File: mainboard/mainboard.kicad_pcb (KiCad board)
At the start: 2 copper layers, 116.8 x 73.7 mm, 26 parts, among them J1 Port ESC Connector, J2 Stbd ESC Connector, J3 Battery Connector, J4 RPLIDAR Power Harness, J5 Raspberry_Pi_4

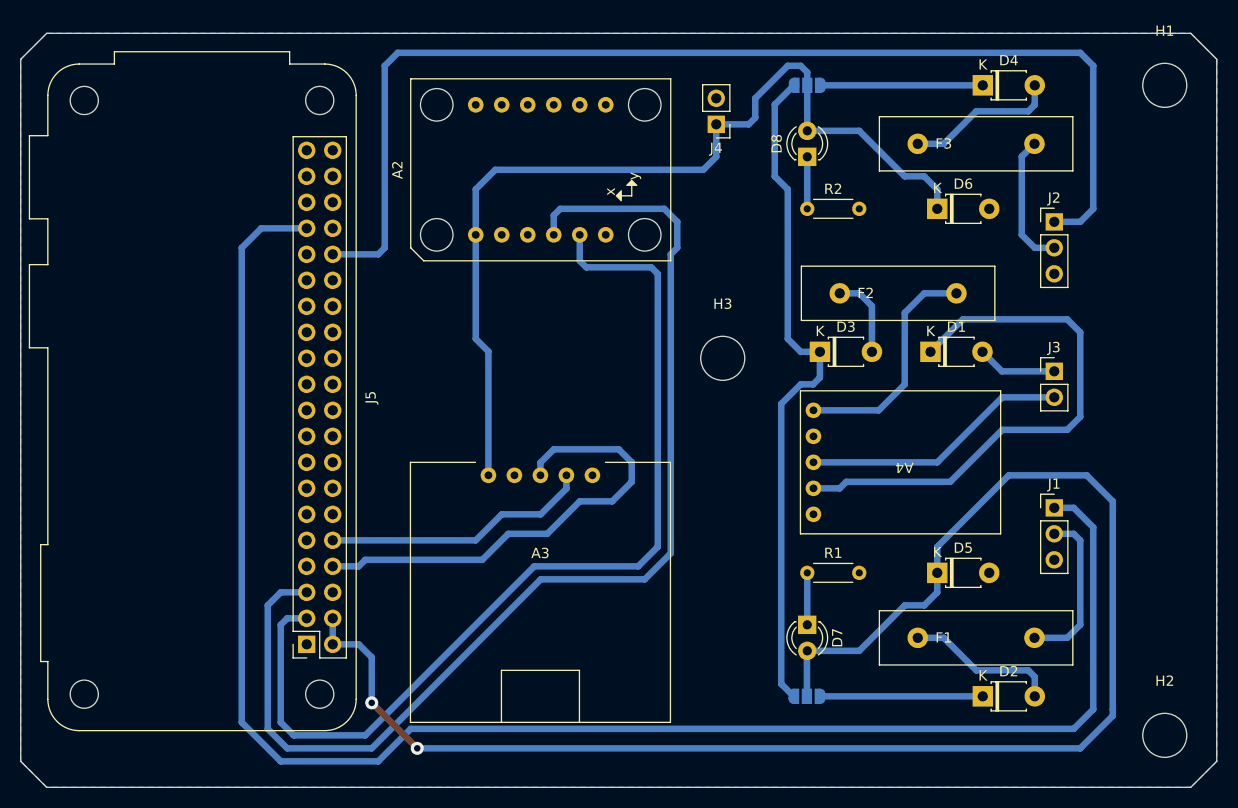
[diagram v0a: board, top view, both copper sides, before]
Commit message: Updated pcb to in spec
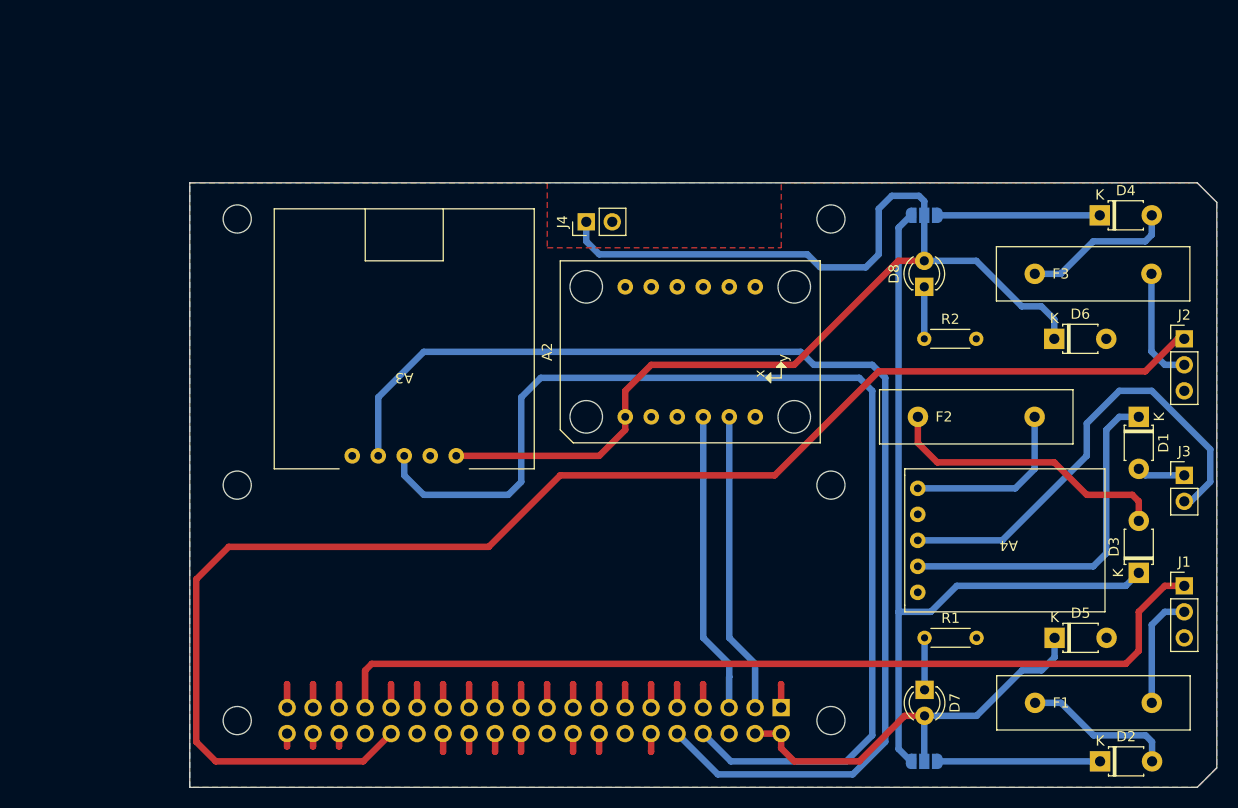
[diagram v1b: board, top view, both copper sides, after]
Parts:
- removed H1, H2, H3: MountingHole, MountingHole:MountingHole_4.3mm_M4
- J5: footprint Module:Raspberry_Pi_Zero_Socketed_THT_FaceDown_MountingHoles -> GTMRG_footprints:RaspberryPi_Multi; moved to B.Cu
- moved D3 37.9 mm to (203.8, 108.6), turned to 90 degrees
- moved A3 28.1 mm to (132.1, 85.7), turned to 180 degrees
- moved A2 23.0 mm to (160.0, 87.0)
- moved J5 22.9 mm to (144.8, 109.9), turned to 90 degrees
- moved D1 21.3 mm to (203.8, 93.3), turned to -90 degrees
- moved D8 17.1 mm to (182.9, 80.6)
- moved D4 17.1 mm to (200.0, 73.7)
- moved JP2 17.1 mm to (182.9, 73.7)
- moved D6 17.1 mm to (195.6, 85.7)
- moved R2 17.1 mm to (182.9, 85.7)
- moved F3 17.1 mm to (205.1, 79.4)
- moved J2 17.1 mm to (208.3, 85.7)
- moved J3 16.3 mm to (208.3, 99.1)
- moved J4 15.9 mm to (149.9, 74.3), turned to 90 degrees
- moved J1 14.8 mm to (208.3, 109.9)
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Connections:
- J5 pad 1: Net-(J5-3V3-Pad1) -> unconnected-(J5-3V3-Pad1)_1
- J5 pad 17: Net-(J5-3V3-Pad1) -> unconnected-(J5-3V3-Pad1)
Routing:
- net +5V_P: track 152.9 -> 41.8 mm, vias 2 -> 0
- net /GPS_TX: track 26.2 -> 117.0 mm
- net /SCL: track 111.9 -> 29.5 mm
- net /PEsc_Sig: track 162.7 -> 89.3 mm
- net /SDA: track 94.7 -> 29.5 mm
- net /GPS_RX: track 45.8 -> 110.9 mm
- net /SEsc_Sig: track 111.7 -> 143.1 mm
- net +5V_S: track 91.8 -> 120.3 mm
- net Net-(D3-A): track 8.13 -> 28.4 mm
- net Net-(A4-IN-): track 26.2 -> 45.4 mm
- net Net-(A4-IN+): track 53.7 -> 34.7 mm
- net Net-(D3-K): track 66.2 -> 79.4 mm
- net GND: track 0.00 -> 6.88 mm
- net +5V_Reg: track 22.8 -> 17.3 mm
- net +5V_PEsc: track 16.1 -> 11.3 mm
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- added copper zone on F.Cu, net GND
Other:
- board size 116.8 x 73.7 mm -> 100.3 x 59.1 mm
- board text removed: "Full Raspberry Pi Approximate Dimensions"

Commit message: Updated to a fabbed PCB
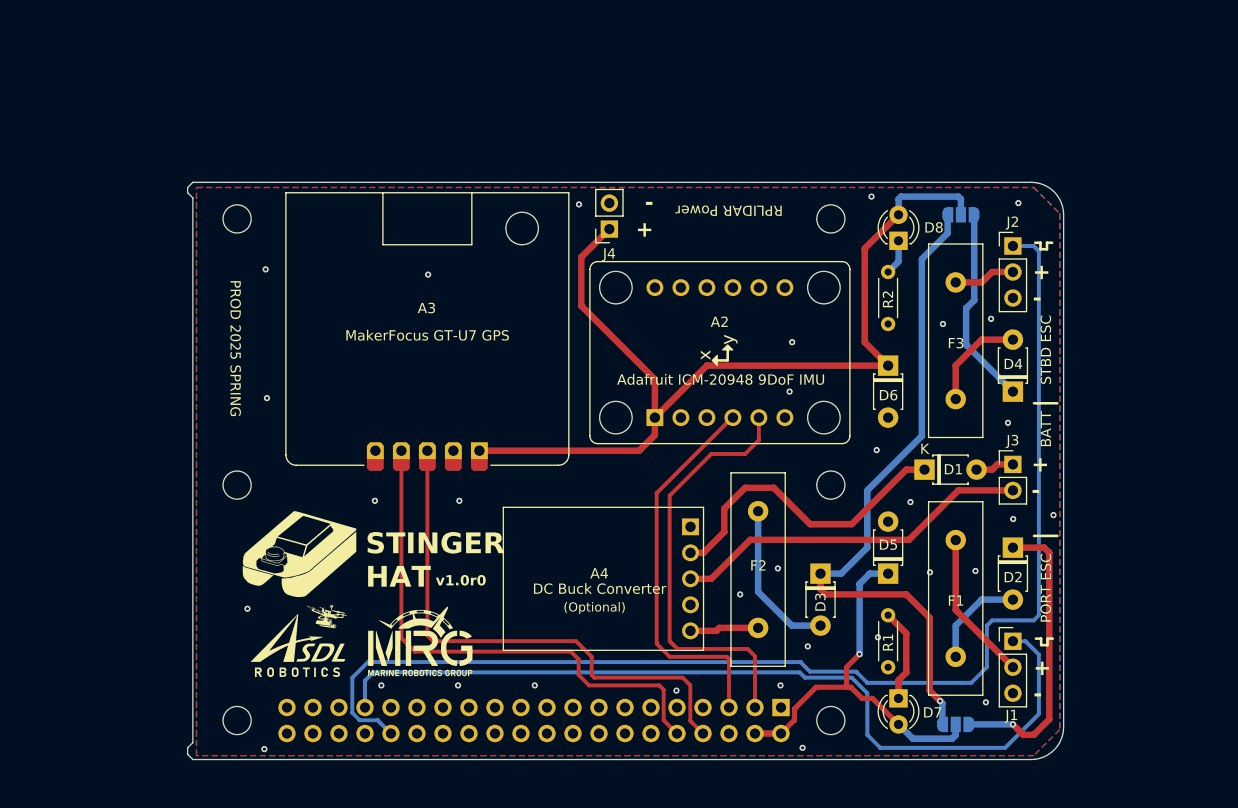
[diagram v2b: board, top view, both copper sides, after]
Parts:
- A4: value DROK DC Buck Converter -> DC Buck Converter
- J4: footprint Connector_PinHeader_2.54mm:PinHeader_1x02_P2.54mm_Vertical -> Connector_PinSocket_2.54mm:PinSocket_1x02_P2.54mm_Vertical
- moved A4 40.2 mm to (151.2, 109.2), turned to 0 degrees
- moved F2 34.0 mm to (166.6, 114.0), turned to 90 degrees
- moved D3 31.1 mm to (172.7, 108.7), turned to -90 degrees
- moved F1 24.9 mm to (186.0, 105.4), turned to -90 degrees
- moved D2 22.5 mm to (191.5, 106.1), turned to -90 degrees
- moved D1 21.6 mm to (182.9, 98.5), turned to 0 degrees
- moved D4 19.2 mm to (191.5, 90.9), turned to 90 degrees
- moved F3 19.1 mm to (186.0, 80.2), turned to -90 degrees
- moved J2 19.0 mm to (191.5, 76.7)
- moved J1 17.6 mm to (191.5, 115.3)
- moved D5 17.4 mm to (179.3, 108.7), turned to 90 degrees
- moved J3 16.8 mm to (191.5, 98.0)
- moved D6 16.4 mm to (179.3, 88.3), turned to -90 degrees
- moved R2 7.42 mm to (179.3, 79.2), turned to -90 degrees
- moved D8 5.15 mm to (180.4, 76.1)
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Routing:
- net /GPS_TX: track 117.0 -> 50.4 mm
- net /GPS_RX: track 110.9 -> 50.7 mm
- net +5V_S: track 120.3 -> 93.3 mm
- net /SEsc_Sig: track 143.1 -> 120.0 mm
- net Net-(D3-K): track 79.4 -> 65.7 mm, vias 0 -> 1
- net Net-(D3-A): track 28.4 -> 15.3 mm
- net Net-(D2-K): track 15.9 -> 28.9 mm, vias 0 -> 1
- net /SDA: track 29.5 -> 41.3 mm
- net +5V_Reg: track 17.3 -> 6.72 mm
- net Net-(A4-IN-): track 45.4 -> 35.1 mm
- net /SCL: track 29.5 -> 37.6 mm
- net GND: track 6.88 -> 0.00 mm, vias 0 -> 32
- net +5V_SEsc: track 11.3 -> 6.01 mm
- net Net-(D2-A): track 14.9 -> 9.69 mm
- net Net-(D4-A): track 14.9 -> 9.91 mm
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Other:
- board size 100.3 x 59.1 mm -> 85.6 x 56.4 mm
- board text added: "(Optional)"
- board text added: "+"
- board text added: "-"
- board text added: "BATT"
- board text added: "ESC|OUT|REG"
- board text added: "PORT ESC"
- board text added: "PROD 2025 SPRING"
- board text added: "REG|OUT|ESC"
- board text added: "RPLIDAR Power"
- board text added: "STBD ESC"
- board text added: "STINGER HAT"
- board text added: "v1.0r0"
